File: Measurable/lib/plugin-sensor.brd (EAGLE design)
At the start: 160 x 100 mm, 3 parts

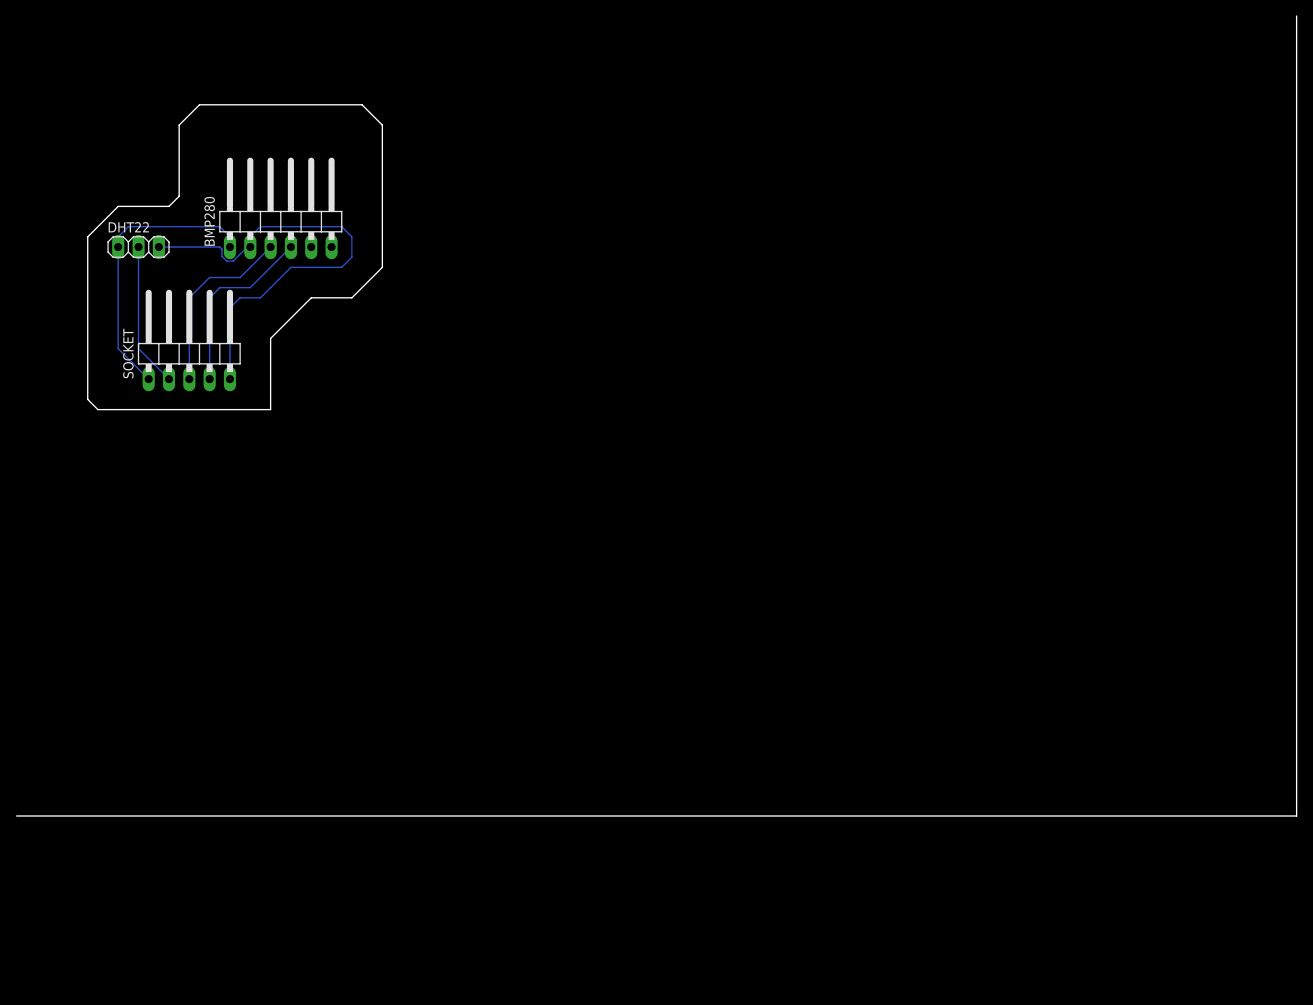
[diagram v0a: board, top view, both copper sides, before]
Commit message: update measurable sensor
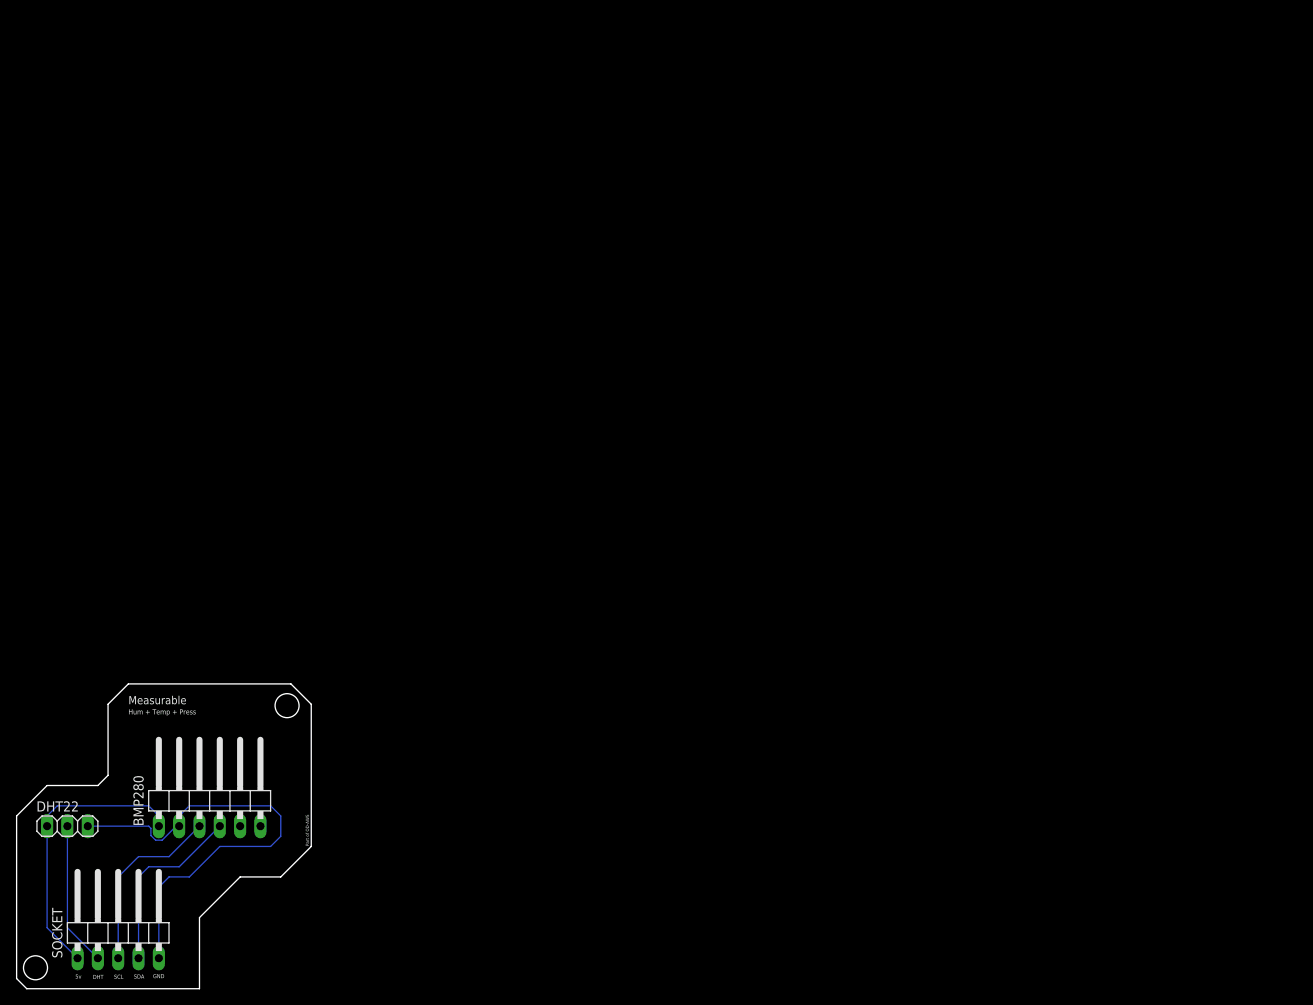
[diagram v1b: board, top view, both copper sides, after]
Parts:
- moved BMP280 72.9 mm to (24.1, 2.54)
- moved DHT22 72.9 mm to (6.35, -1.27)
- moved SOCKET 72.9 mm to (12.7, -14.0)
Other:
- board size 160 x 100 mm -> 36.8 x 38.1 mm
- board text added: "Hum + Temp + Press"
- board text added: "Measurable"
- board text added: "Part of OD-AWS"
- board text removed: "Humadity + Temprature + Air Pressure"
- board text removed: "OD-AWS"
